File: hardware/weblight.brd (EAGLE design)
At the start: 31.8 x 12 mm, 14 parts, among them U1 ATtiny85-20SU

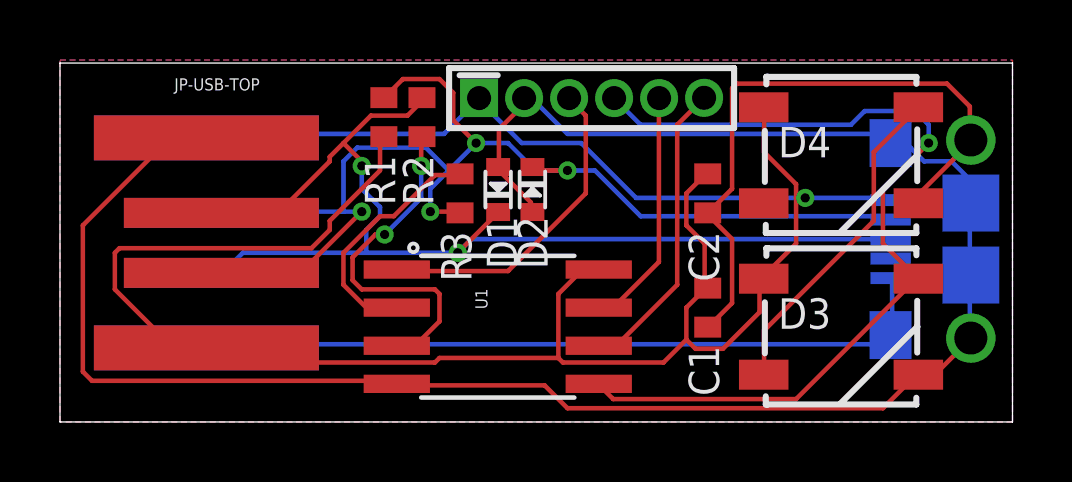
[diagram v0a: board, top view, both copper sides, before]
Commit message: #2: Remove bottom USB connector to avoid short
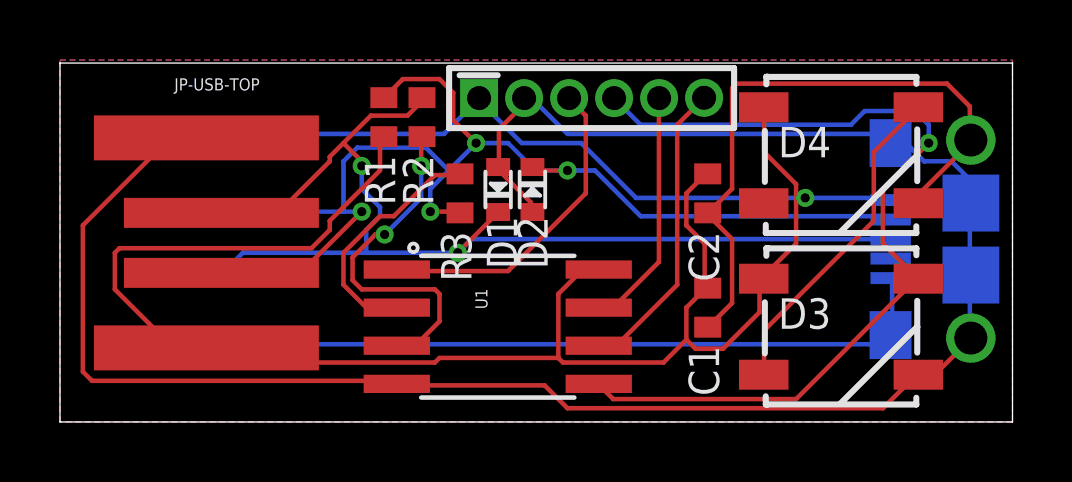
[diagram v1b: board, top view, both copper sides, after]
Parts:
- removed JP-USB-BOT: USBPCB, SparkFun-Connectors:USB-A-PCB
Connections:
- net GND: no longer JP-USB-BOT.GND
- net USB_D_MINUS_RAW: no longer JP-USB-BOT.USB_M
- net USB_D_PLUS_RAW: no longer JP-USB-BOT.USB_P
- net VCC: no longer JP-USB-BOT.5V
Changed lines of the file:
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@@
 <attribute name="VALUE" x="30.289" y="7.29" size="0.6096" layer="27"/>
-</element>
-<element name="JP-USB-BOT" library="SparkFun-Connectors" package="USB-A-PCB" value="USBPCB" x="5.08" y="5.969" smashed="yes" rot="MR180">
-<attribute name="NAME" x="3.81" y="0.889" size="0.4064" layer="26" rot="MR180"/>
-<attribute name="VALUE" x="3.81" y="11.049" size="0.4064" layer="28" rot="MR180"/>
 </element>
 <element name="U1" library="SparkFun-DigitalIC" package="SO08-EIAJ" value="ATtiny85-20SU" x="14.605" y="3.175" rot="R270">
@@
 <contactref element="JP-USB-TOP" pad="5V"/>
 <contactref element="R1" pad="2"/>
-<contactref element="JP-USB-BOT" pad="5V"/>
 <contactref element="JP-USB-MICRO" pad="1"/>
 <contactref element="JP-ISP" pad="1"/>
@@
 <wire x1="12.8016" y1="9.6012" x2="5.0292" y2="9.6012" width="0.1524" layer="16"/>
 <wire x1="13.8684" y1="10.668" x2="12.8016" y2="9.6012" width="0.1524" layer="16"/>
-<wire x1="5.0292" y1="9.6012" x2="4.88" y2="9.469" width="0.1524" layer="16"/>
 <wire x1="13.8684" y1="10.668" x2="13.97" y2="10.795" width="0.1524" layer="16"/>
 <wire x1="24.8412" y1="7.4676" x2="24.5364" y2="7.4676" width="0.1524" layer="1"/>
@@
 <contactref element="D1" pad="A"/>
 <contactref element="D4" pad="3"/>
-<contactref element="JP-USB-BOT" pad="GND"/>
 <contactref element="U1" pad="4"/>
 <contactref element="JP-USB-MICRO" pad="5"/>
@@
 <wire x1="27.2796" y1="2.5908" x2="5.0292" y2="2.5908" width="0.1524" layer="16"/>
 <wire x1="27.5844" y1="2.8956" x2="27.2796" y2="2.5908" width="0.1524" layer="16"/>
-<wire x1="5.0292" y1="2.5908" x2="4.88" y2="2.469" width="0.1524" layer="16"/>
 <wire x1="27.5844" y1="2.8956" x2="27.686" y2="2.896" width="0.1524" layer="16"/>
 <wire x1="3.6576" y1="9.4488" x2="4.8768" y2="9.4488" width="0.1524" layer="1"/>
@@
 <contactref element="R1" pad="1"/>
 <contactref element="D2" pad="K"/>
-<contactref element="JP-USB-BOT" pad="USB_M"/>
 <contactref element="JP-USB-MICRO" pad="2"/>
 <wire x1="8.0772" y1="5.0292" x2="5.4864" y2="5.0292" width="0.1524" layer="1"/>
@@
 <wire x1="9.4488" y1="7.0104" x2="10.0584" y2="7.0104" width="0.1524" layer="16"/>
 <wire x1="5.4864" y1="5.0292" x2="5.38" y2="4.969" width="0.1524" layer="1"/>
-<wire x1="5.4864" y1="7.0104" x2="5.38" y2="6.969" width="0.1524" layer="16"/>
 <wire x1="16.9164" y1="8.382" x2="15.8496" y2="8.382" width="0.1524" layer="1"/>
 <wire x1="17.8308" y1="8.382" x2="16.9164" y2="8.382" width="0.1524" layer="16"/>
@@
 <contactref element="R2" pad="1"/>
 <contactref element="D1" pad="K"/>
-<contactref element="JP-USB-BOT" pad="USB_P"/>
 <contactref element="JP-USB-MICRO" pad="3"/>
 <wire x1="11.5824" y1="10.2108" x2="12.0396" y2="10.668" width="0.1524" layer="1"/>
@@
 <wire x1="5.4864" y1="5.0292" x2="6.096" y2="5.6388" width="0.1524" layer="16"/>
 <wire x1="14.478" y1="6.858" x2="14.605" y2="6.997" width="0.1524" layer="1"/>
-<wire x1="5.4864" y1="5.0292" x2="5.38" y2="4.969" width="0.1524" layer="16"/>
 <wire x1="13.716" y1="6.096" x2="27.686" y2="6.096" width="0.1524" layer="16"/>
 <wire x1="13.2588" y1="5.6388" x2="13.716" y2="6.096" width="0.1524" layer="16"/>

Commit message: #17: add 470 ohm resistor before first DIN
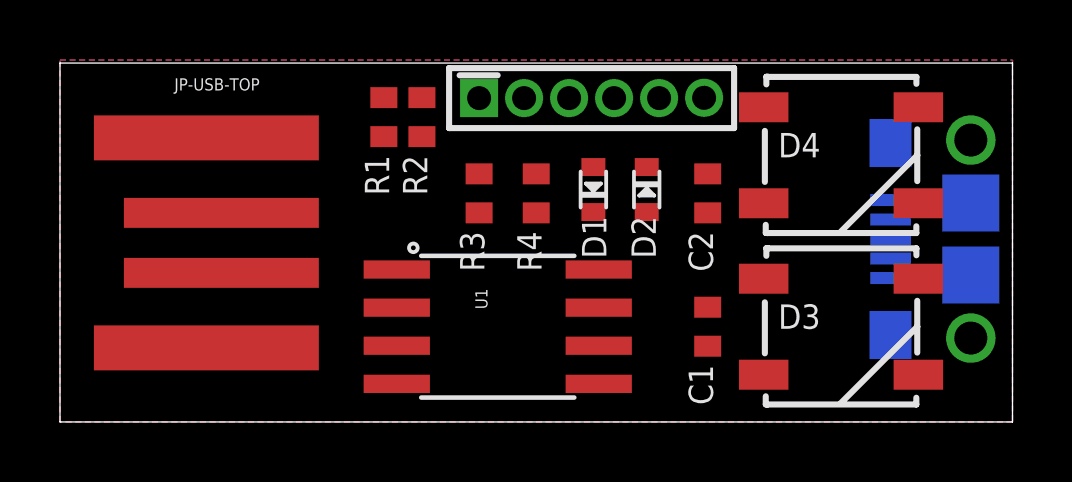
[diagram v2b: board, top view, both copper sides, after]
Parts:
- added R4: 470, rcl:R0402
- moved D2 3.81 mm to (19.6, 7.75)
- moved D1 3.18 mm to (17.8, 7.75)
- moved C1 0.64 mm to (21.6, 3.17)
- moved R3 0.63 mm to (14.0, 7.62)
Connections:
- new net N$1: D3.4, R4.1
- new net SLD: JP-USB-MICRO.S1, JP-USB-MICRO.S2, JP-USB-MICRO.S3, JP-USB-MICRO.S4, JP-USB-MICRO.S5, JP-USB-MICRO.S6
- net GND: no longer JP-USB-MICRO.S1, JP-USB-MICRO.S2, JP-USB-MICRO.S3, JP-USB-MICRO.S4, JP-USB-MICRO.S5, JP-USB-MICRO.S6
- net MOSI/DIN: now also R4.2; no longer D3.4
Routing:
- net GND: track 117.0 -> 0.00 mm
- net VCC: track 79.2 -> 0.00 mm, vias 1 -> 0
- net USB_D_MINUS_RAW: track 40.5 -> 0.00 mm, vias 4 -> 0
- net USB_D_PLUS_RAW: track 37.3 -> 0.00 mm, vias 2 -> 0
- net MOSI/DIN: track 30.0 -> 0.00 mm, vias 1 -> 0
- net USB_D_PLUS: track 11.7 -> 0.00 mm, vias 2 -> 0
- net DIN_2: track 11.0 -> 0.00 mm
- net RESET: track 10.8 -> 0.00 mm
- net MISO: track 10.1 -> 0.00 mm
- net USB_D_MINUS: track 8.13 -> 0.00 mm
- net SCK: track 8.10 -> 0.00 mm
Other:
- board text added: "Version mf3"
- board text removed: "version mf2"

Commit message: Changes to prod circuit.
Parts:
- removed JP-ISP: AVR_MINI_PROGSMD, SparkFun-Connectors:AVR_MINI_PROG
- added D5, D6: WS2812B, SparkFun-LED:WS2812B
- moved R4 14.7 mm to (30.5, 6.10), turned to 90 degrees
- moved D2 4.58 mm to (15.7, 10.3)
- moved D1 4.07 mm to (14.6, 10.3)
- moved R3 2.62 mm to (13.3, 10.2)
- moved C2 1.27 mm to (21.6, 8.89)
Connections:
- removed net MISO: JP-ISP.6, U1.6
- removed net RESET: JP-ISP.3, U1.1
- removed net SCK: JP-ISP.5, U1.7
- new net N$2: D5.2, D6.4
- new net N$3: D4.2, D5.4
- net GND: now also D5.3, D6.3; no longer JP-ISP.2
- net MOSI/DIN: no longer JP-ISP.4
- net USB_D_MINUS: now also R3.1; no longer R3.2
- net USB_D_MINUS_RAW: now also R3.2; no longer R3.1
- net VCC: now also D5.1, D6.1; no longer JP-ISP.1
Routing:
- net GND: track 0.00 -> 69.8 mm, vias 0 -> 2
- net VCC: track 0.00 -> 65.0 mm, vias 0 -> 2
- net USB_D_MINUS_RAW: track 0.00 -> 39.4 mm, vias 0 -> 1
- net USB_D_PLUS_RAW: track 0.00 -> 36.5 mm, vias 0 -> 3
- net MOSI/DIN: track 0.00 -> 16.1 mm
- net SLD: track 0.00 -> 11.9 mm
- net N$2: track 0.00 -> 11.1 mm
- net DIN_2: track 0.00 -> 11.0 mm
- net USB_D_PLUS: track 0.00 -> 8.82 mm
- net USB_D_MINUS: track 0.00 -> 6.88 mm
- net N$3: track 0.00 -> 5.17 mm, vias 0 -> 1
- net N$1: track 0.00 -> 2.24 mm

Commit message: Fix net names.
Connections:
- net MOSI/DIN renamed DIN_RAW
- net N$1 renamed DIN_1
- net N$2 renamed DIN_4
- net N$3 renamed DIN_3
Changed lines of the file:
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@@
 </polygon>
 </signal>
-<signal name="MOSI/DIN">
+<signal name="DIN_RAW">
 <contactref element="U1" pad="5"/>
 <contactref element="R4" pad="2"/>
@@
 <wire x1="28.4988" y1="10.3632" x2="28.612" y2="10.49" width="0.1524" layer="1"/>
 </signal>
-<signal name="N$1">
+<signal name="DIN_1">
 <contactref element="D3" pad="4"/>
 <contactref element="R4" pad="1"/>
@@
 <wire x1="30.3276" y1="7.1628" x2="30.361" y2="7.296" width="0.1524" layer="16"/>
 </signal>
-<signal name="N$3">
+<signal name="DIN_3">
 <contactref element="D4" pad="2"/>
 <contactref element="D5" pad="4"/>
@@
 <via x="21.6408" y="5.4864" extent="1-16" drill="0.3048"/>
 </signal>
-<signal name="N$2">
+<signal name="DIN_4">
 <contactref element="D5" pad="2"/>
 <contactref element="D6" pad="4"/>

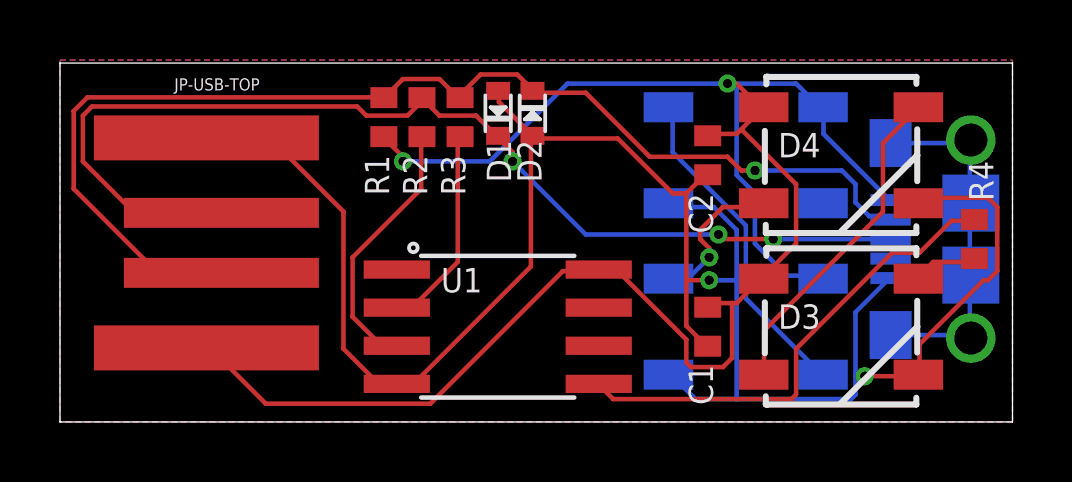
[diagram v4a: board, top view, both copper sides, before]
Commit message: mf3 rc1
Pullup resistor on NRES
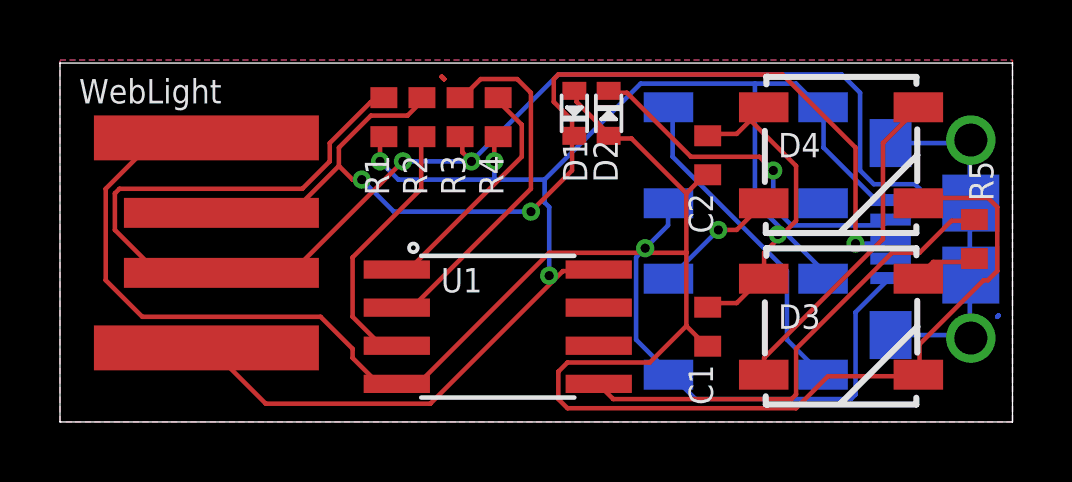
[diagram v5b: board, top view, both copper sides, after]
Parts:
- added R5: 470, rcl:R0402
- R4: value 470 -> 4.7K
- moved R4 16.4 mm to (14.6, 10.2)
- moved D2 2.54 mm to (18.3, 10.3)
- moved D1 2.54 mm to (17.1, 10.3)
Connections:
- new net N_RESET: R4.2, U1.1
- net DIN_1: now also R5.1; no longer R4.1
- net DIN_RAW: now also R5.2; no longer R4.2
- net USB_D_MINUS: now also R3.2; no longer R3.1
- net USB_D_MINUS_RAW: now also R3.1; no longer R3.2
- net VCC: now also R4.1
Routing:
- net USB_D_MINUS_RAW: track 39.4 -> 60.0 mm, vias 1 -> 3
- net GND: track 69.8 -> 87.4 mm, vias 2 -> 1
- net N_RESET: track 0.00 -> 8.03 mm
- net USB_D_MINUS: track 6.88 -> 12.1 mm
- net VCC: track 65.0 -> 61.9 mm, vias 2 -> 4
- net DIN_3: track 5.17 -> 4.20 mm
- net N$2: track 0.00 -> 0.63 mm
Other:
- board text added: "WebLight"
